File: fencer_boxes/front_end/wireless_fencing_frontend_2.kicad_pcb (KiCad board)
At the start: 2 copper layers, 16.8 x 22.8 mm, 18 parts, among them J1 Conn_01x03, J2 Conn_01x08, U2 AD8619

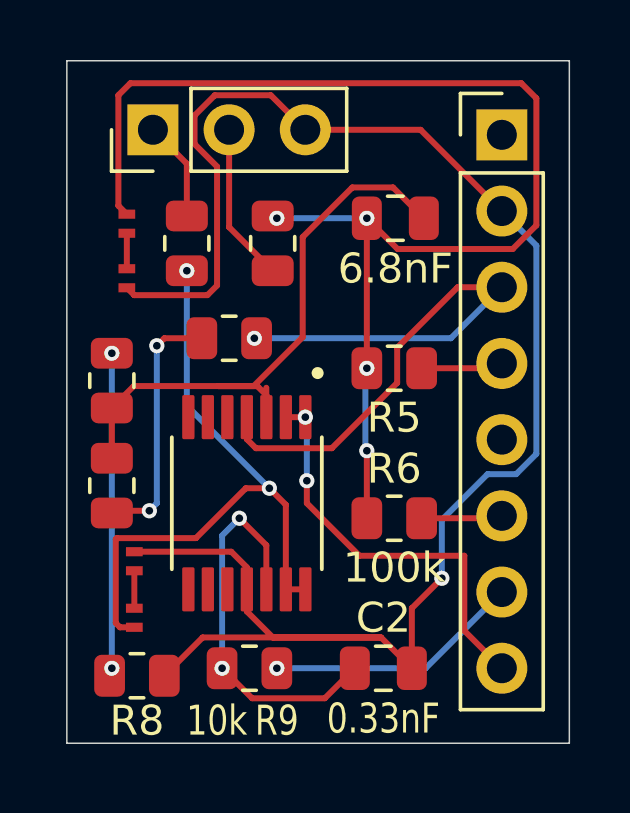
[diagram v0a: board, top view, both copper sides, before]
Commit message: front end tvs and resistor combination
* Single SOD-523 footprint for TVS diodes
* Changed from using 2x20kOhm in series to single 40kOhm.
Initially was trying to minimize the number of different values, but resistors
are like a cent a piece, even in pretty small quantities, and this saves soldering.
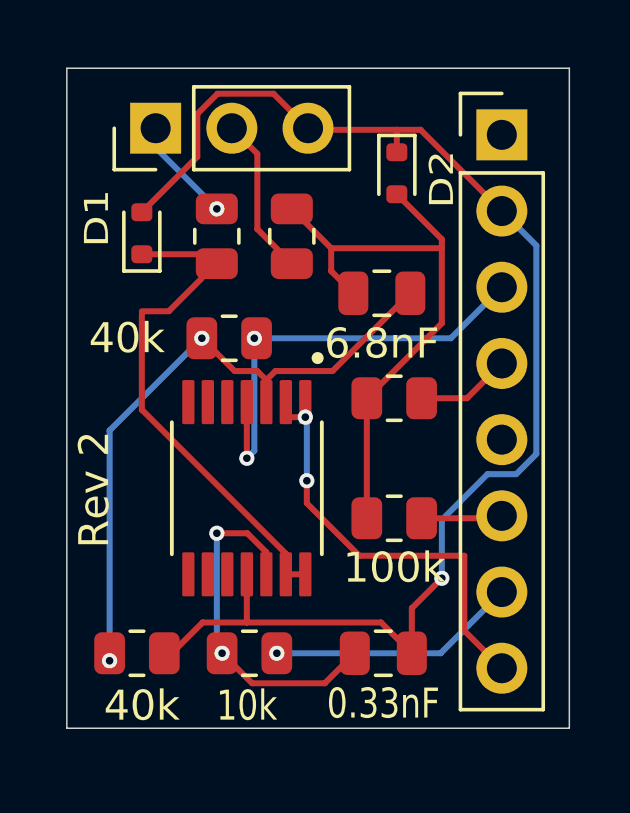
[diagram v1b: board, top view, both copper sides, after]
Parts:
- removed CR1, CR2, CR3, CR4: ESDALC6V1-1M2, ESDALC6V1:SOD882_STM
- removed R2, R3: 20k, Resistor_SMD:R_0805_2012Metric
- added D1: SLESD5491S, Diode_SMD:D_SOD-523, F.Cu at (148.5, 67.5)
- added D2: SLESD5491S, Diode_SMD:D_SOD-523, F.Cu at (157.0, 65.5)
- R7, R8: value 20k -> 40k
- moved C1 2.54 mm to (156.5, 69.5)
- moved R4 1.03 mm to (151.0, 67.6)
- moved R5 1.00 mm to (156.9, 73.0)
- moved R8 0.75 mm to (148.3, 81.5)
- moved R1 0.68 mm to (153.5, 67.6)
- moved C2 0.50 mm to (156.6, 81.5)
- moved R9 0.50 mm to (152.1, 81.5)
- moved U2 0.50 mm to (152.0, 76.0)
- moved J1 0.10 mm to (149.0, 64.0)
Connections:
- R7 pad 1: Net-(R2-Pad2) -> Net-(U2-+IN_A)
- R8 pad 2: Net-(R3-Pad1) -> Net-(U2-+IN_A)
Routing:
- net Net-(D2-A2): track 42.2 -> 19.9 mm, vias 4 -> 0
- net Earth: track 58.8 -> 45.7 mm
- net Net-(R3-Pad1): track 10.8 -> 0.00 mm, vias 2 -> 0
- net Net-(R2-Pad2): track 8.49 -> 0.00 mm, vias 2 -> 0
- net +3.3V: track 21.3 -> 15.0 mm, vias 1 -> 2
- net Net-(D1-A1): track 21.9 -> 16.4 mm, vias 2 -> 0
- net Net-(U2-+IN_D): track 13.2 -> 12.0 mm
- net Net-(CR3-K): track 1.25 -> 0.00 mm
- net Net-(CR1-K): track 1.18 -> 0.00 mm
- net Net-(U2-+IN_A): track 22.2 -> 23.2 mm, vias 0 -> 2
- net Net-(J1-Pin_1): track 3.34 -> 3.53 mm, vias 0 -> 1
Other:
- board size 16.8 x 22.8 mm -> 16.8 x 22 mm
- board text added: "Rev 2"

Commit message: Adding simple passive lowpass before  adc buffer
set to 10k, 1nF i.e. f0 16kHz ; used 11k, not critical.

i've bodged this into the existing boards.
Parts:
- added C3: 1nF, Capacitor_SMD:C_0805_2012Metric, F.Cu at (147.3, 74.3)
- added R2: 10k, Resistor_SMD:R_0805_2012Metric, F.Cu at (147.3, 78.2)
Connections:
- C1 pad 2: Net-(U2-+IN_A) -> Net-(C1-Pad2)
- R7 pad 1: Net-(U2-+IN_A) -> Net-(C1-Pad2)
- R8 pad 2: Net-(U2-+IN_A) -> Net-(C1-Pad2)
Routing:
- net Net-(C1-Pad2): track 0.00 -> 20.4 mm, vias 0 -> 2
- net Net-(U2-+IN_A): track 23.2 -> 13.4 mm
- net Earth: track 45.7 -> 52.8 mm
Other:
- board text added: "Rev 3"
- board text removed: "Rev 2"

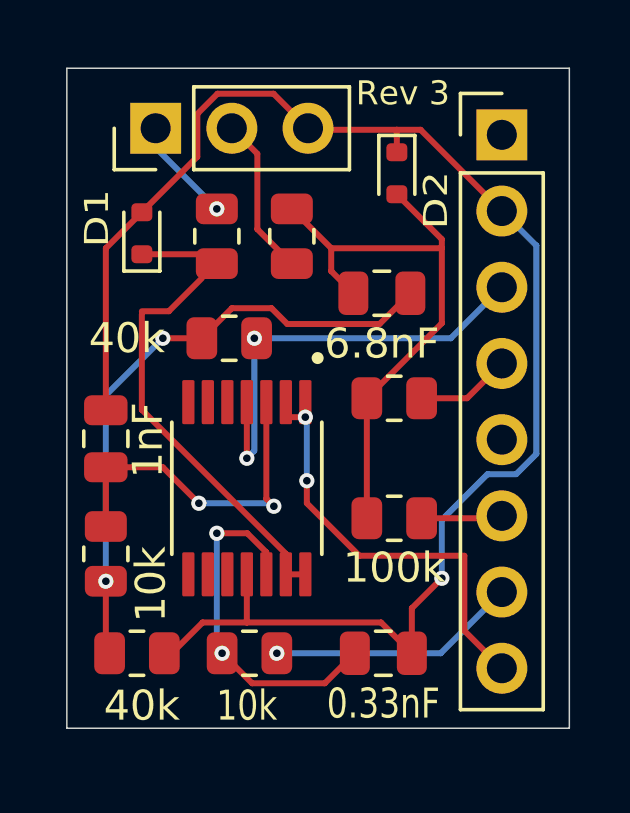
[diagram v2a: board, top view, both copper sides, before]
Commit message: lame drive changed from 20k to 2k
just matching change in reality; not sure if it's important.
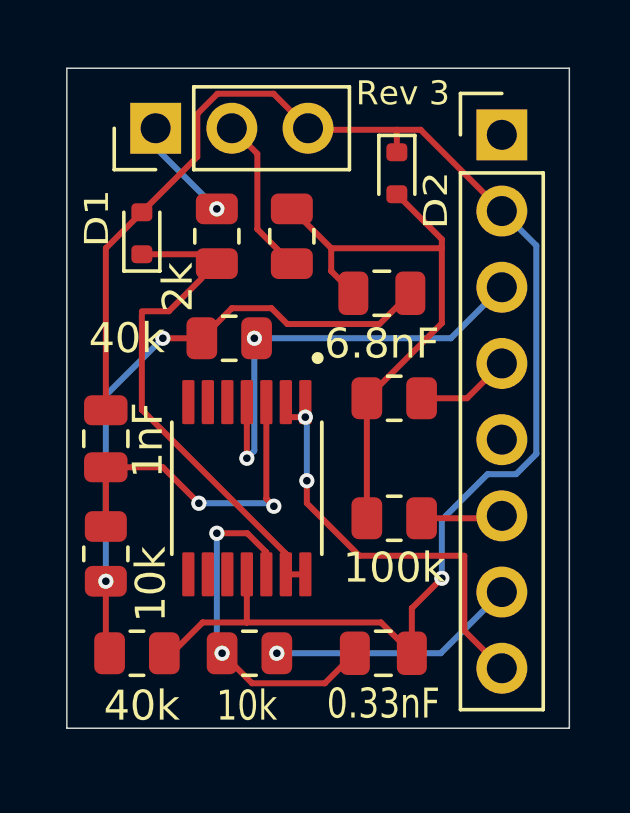
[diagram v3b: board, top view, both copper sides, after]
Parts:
- R4: value 20k -> 2k
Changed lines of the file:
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@@
 			)
 		)
-		(property "Value" "20k"
-			(at -0.0365 -1.551 90)
+		(property "Value" "2k"
+			(at -1.7 -1.3 90)
 			(layer "F.SilkS")
-			(hide yes)
 			(effects
 				(font

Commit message: Adding lame pulldown and common line to ground resistor
so now the lame connection is
1. on a voltage divider between the drive and ground, not floating.
2. setting this to 100 ohm drive, 200 ohm to ground - so also much stronger than before.
and the C (common) line is not tied directly to ground, but has a 2k resistor.

Overall, this doesn't change the tip detection much, but should make the lame drive more
resistant to the common line touching the lame (cause of e.g. sweaty skin). Before this
changed it from floating to grounded, now it 1. does not connect it directly to ground,
but only through a 2k resistor, and 2. the drive is much stronger and more deterministic,
so this won't change the bias much.
It does mean we're consuming about 15mW more (3.3 V over 300 ohm, at 50% duty cycle)
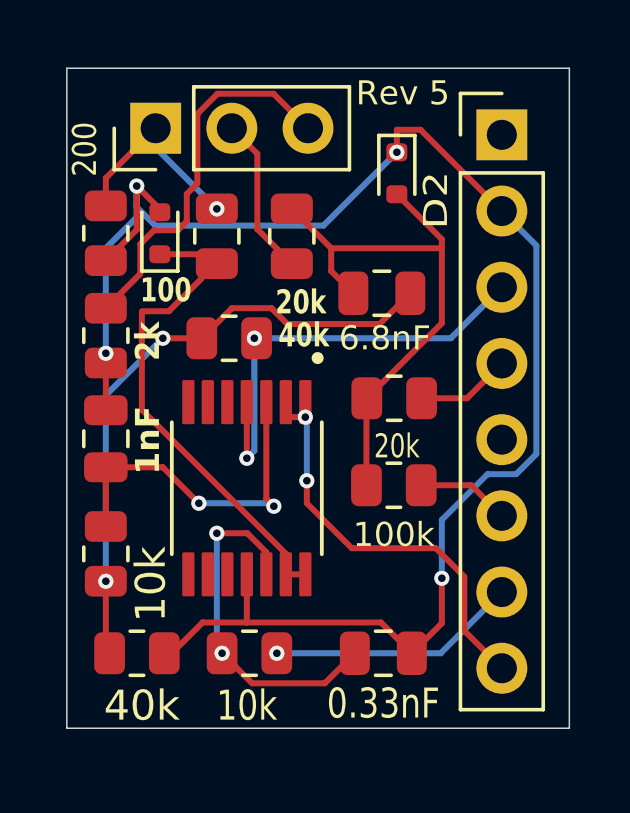
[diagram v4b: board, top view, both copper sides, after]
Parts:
- added R10: 200, Resistor_SMD:R_0805_2012Metric, F.Cu at (147.3, 67.5)
- added R3: 2k, Resistor_SMD:R_0805_2012Metric, F.Cu at (147.3, 70.9)
- R4: value 2k -> 100
- moved R6 1.10 mm to (156.9, 75.9)
- moved D1 0.60 mm to (149.1, 67.5)
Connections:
- J1 pad 3: Earth -> Net-(J1-Pin_3)
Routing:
- net Net-(J1-Pin_3): track 0.00 -> 12.7 mm
- net Earth: track 52.8 -> 56.6 mm, vias 1 -> 4
- net Net-(J1-Pin_1): track 3.53 -> 6.81 mm
- net Net-(D2-A2): track 19.8 -> 18.7 mm
- net Net-(D1-A1): track 16.4 -> 15.8 mm
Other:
- board text added: "Rev 5"
- board text removed: "Rev 3"

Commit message: Change to AC coupling of drive to lame
i.e. add a capacitor on the line.
with the recent addition of tying the lame drive to ground, if one
foil touches the opposite lame, the moment the other touch happens -
 - even before the switch is actually depressed - the voltage at the
pin can be back driven by the (opposite) lame and trigger a false touch.
Braking the DC coupling solves it.
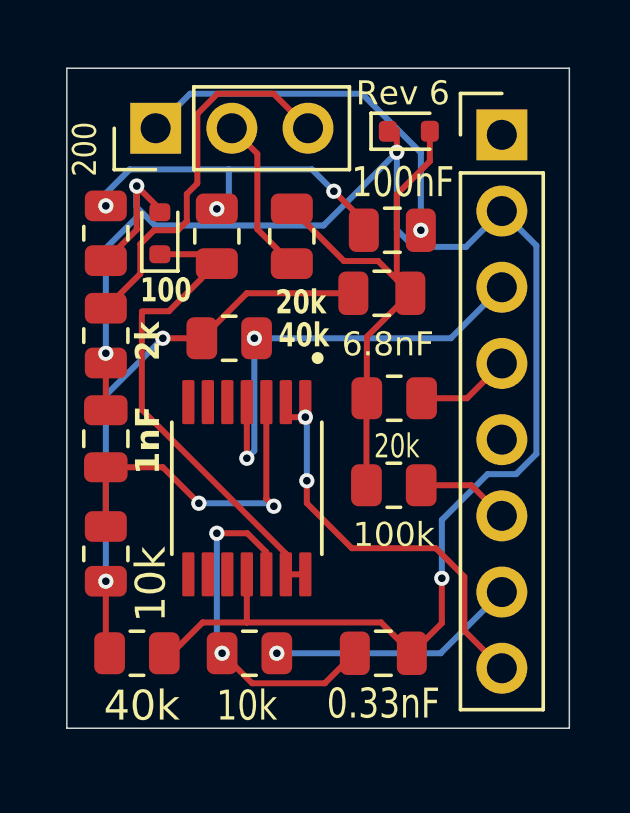
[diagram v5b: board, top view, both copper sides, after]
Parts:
- added C4: 100nF, Capacitor_SMD:C_0805_2012Metric, F.Cu at (156.8, 67.4)
- moved D2 1.46 mm to (157.4, 64.1), turned to 0 degrees
- turned C1 to 180 degrees
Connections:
- R10 pad 2: Net-(J1-Pin_1) -> Net-(C4-Pad2)
- R4 pad 2: Net-(J1-Pin_1) -> Net-(C4-Pad2)
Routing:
- net Net-(C4-Pad2): track 0.00 -> 11.8 mm, vias 0 -> 3
- net Net-(J1-Pin_1): track 6.81 -> 12.7 mm
- net Net-(C1-Pad2): track 20.4 -> 18.1 mm
- net Earth: track 56.6 -> 58.5 mm
- net Net-(D2-A2): track 18.7 -> 18.2 mm
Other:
- board text added: "Rev 6"
- board text removed: "Rev 5"

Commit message: Adjusting lame drive hardware for a stronger drive
* reduce (well, eliminate) the inline resistance (i think not needed
once we're capacitively coupled to the lame)
* increase the capacitor from 100nF to 10uF.

Both of these changes seem to do better when the lame is "shorted" to
the common line; the current configs seem to do ok down to about 5kOhm
of a short, but no lower - so a super sweaty fencer is still an issue,
i think.
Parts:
- C4: value 100nF -> 10uF
- R4: value 100 -> 0
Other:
- board text added: "Rev 7"
- board text removed: "Rev 6"
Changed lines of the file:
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@@
 			)
 		)
-		(property "Value" "100"
+		(property "Value" "0"
 			(at -1.8 -1.7 180)
 			(layer "F.SilkS")
@@
 			)
 		)
-		(property "Value" "100nF"
+		(property "Value" "10uF"
 			(at -0.35 1.6 0)
 			(layer "F.SilkS")
@@
 		(layer "Edge.Cuts")
 	)
-	(gr_text "Rev 6"
+	(gr_text "Rev 7"
 		(at 157.2 63.3 0)
 		(layer "F.SilkS")

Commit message: change lame capacitor to 250 uF
seems to handle sweat etc better
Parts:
- C4: value 10uF -> 250uF
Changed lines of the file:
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@@
 			)
 		)
-		(property "Value" "10uF"
-			(at -0.35 1.6 0)
+		(property "Value" "250uF"
+			(at -0.45 1.6 0)
 			(layer "F.SilkS")
 			(effects
